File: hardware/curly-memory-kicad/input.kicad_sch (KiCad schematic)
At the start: 5 parts

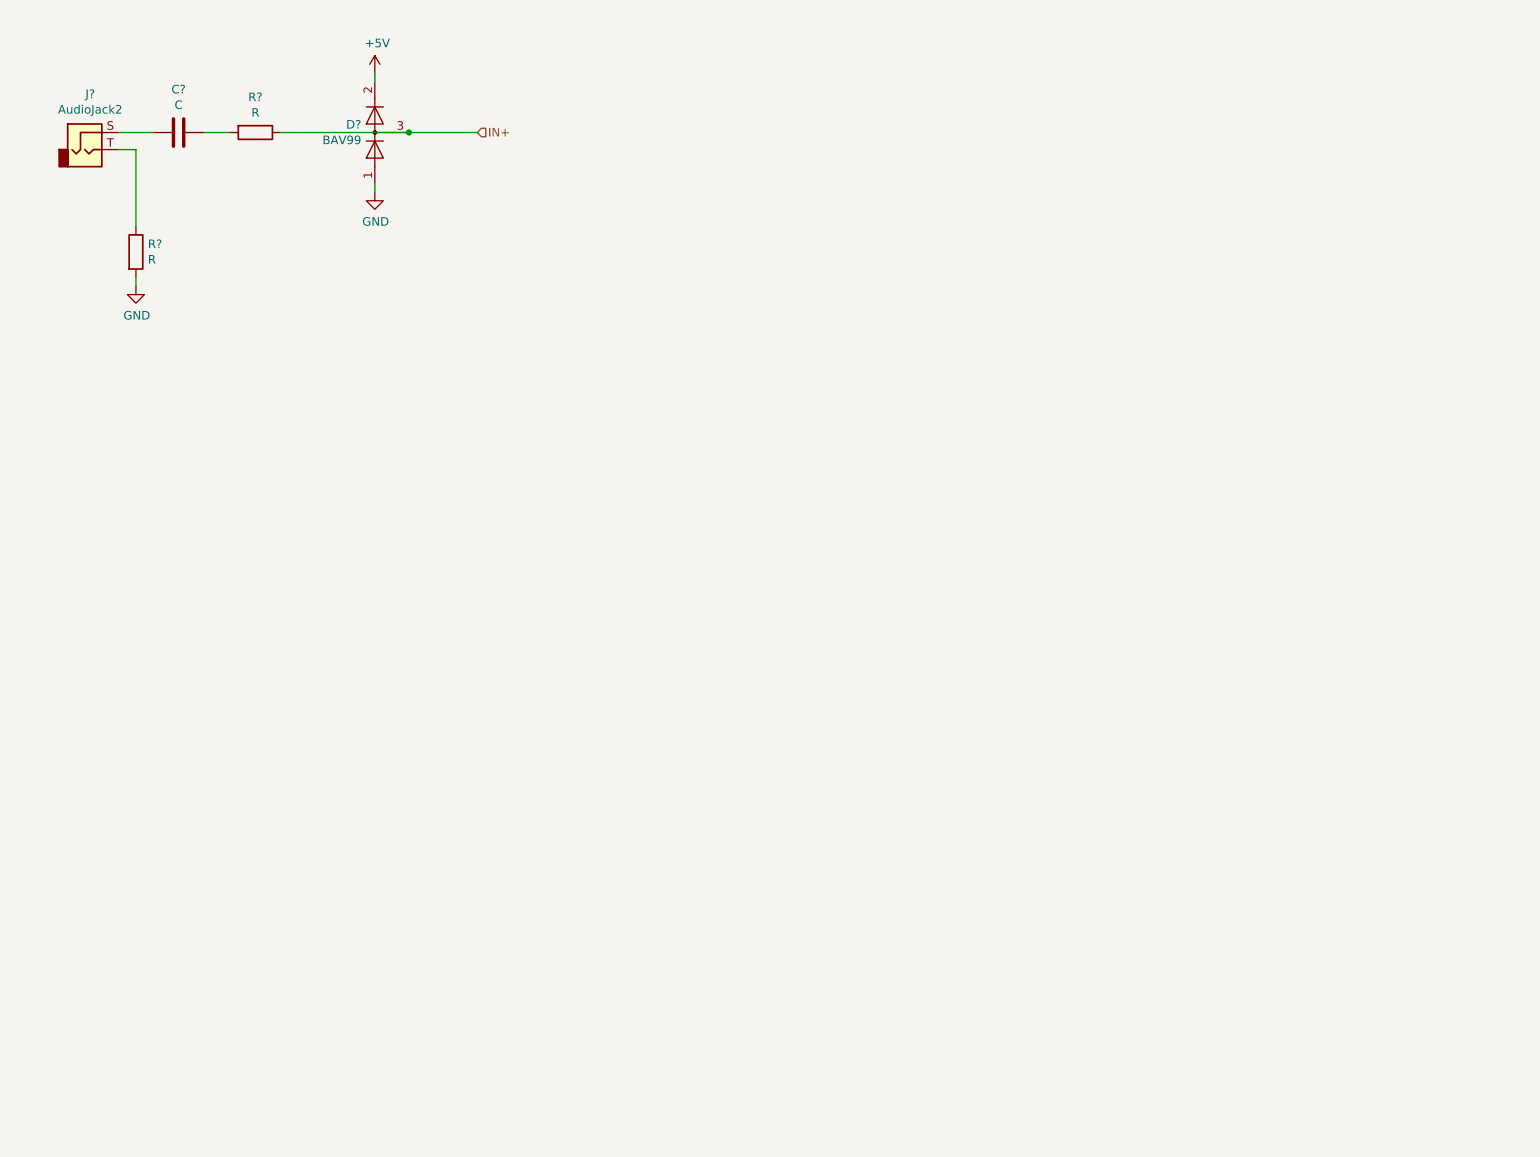
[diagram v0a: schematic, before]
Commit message: output + input op amps added, simuatlion added to sim folder
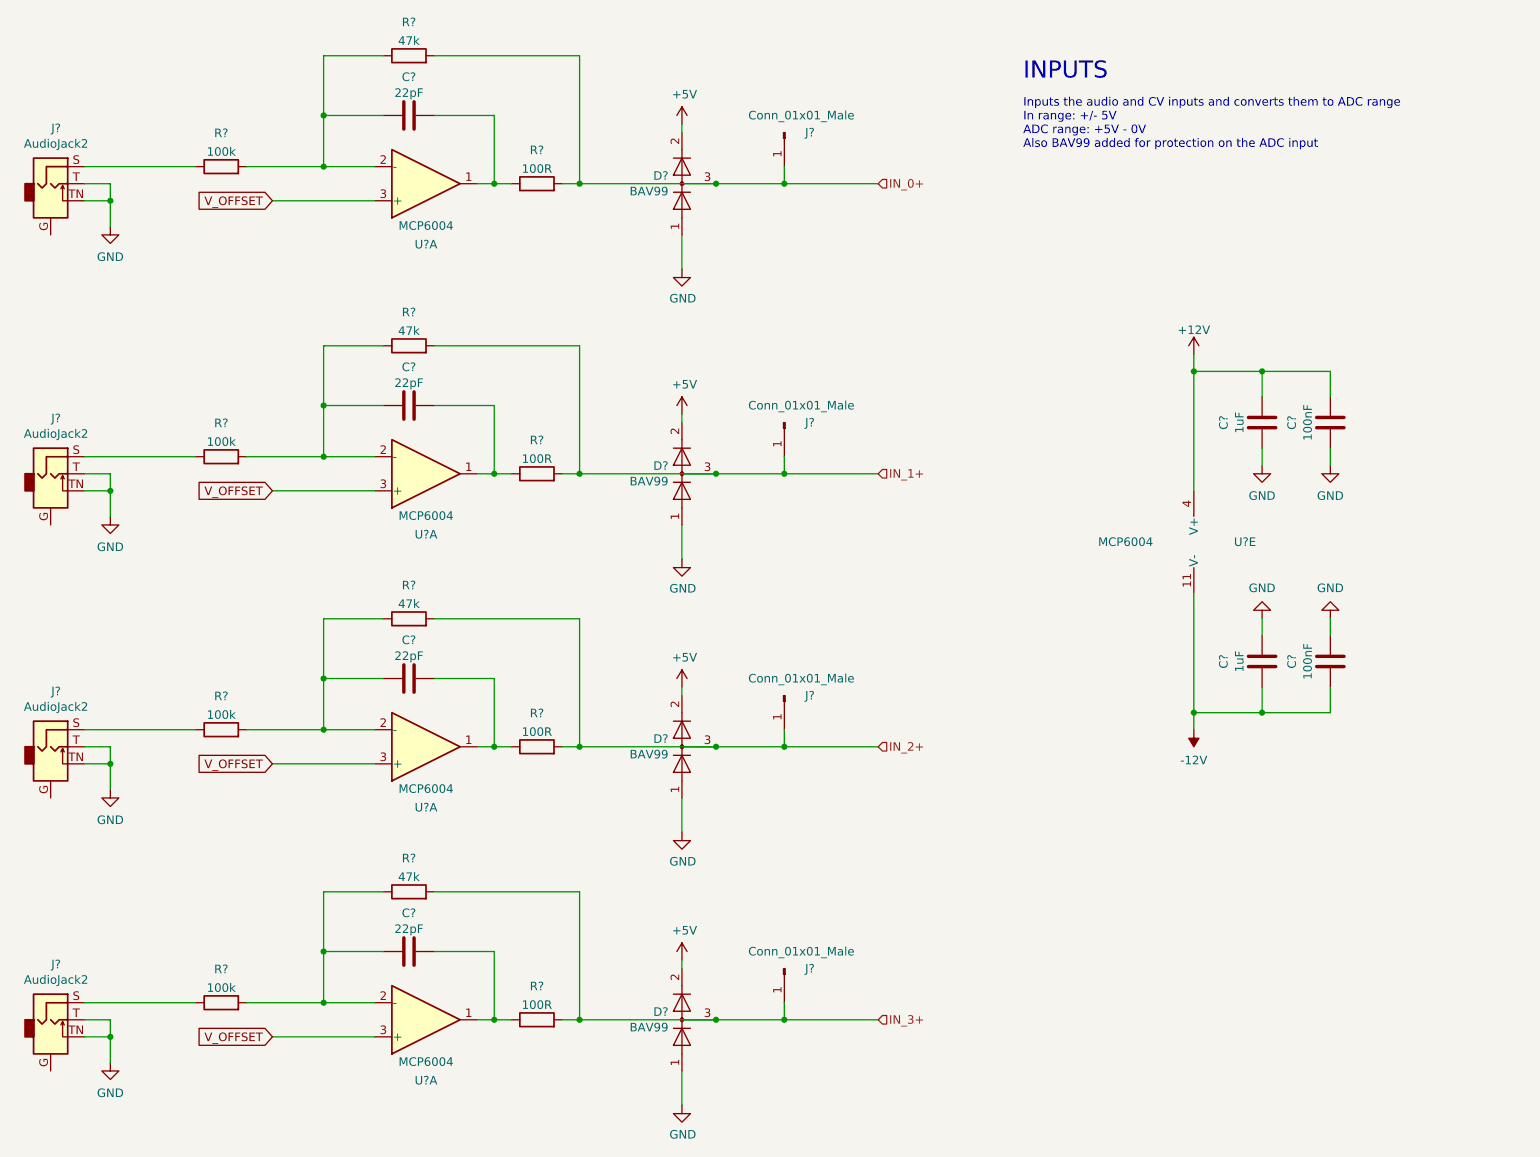
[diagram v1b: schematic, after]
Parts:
- removed C?: C, symbol Device:C
- removed R? (x2): R, symbol Device:R
- added C? (x4): 22pF, symbol Device:C
- added C? (x2): 100nF, symbol Device:C
- added C? (x2): 1uF, symbol Device:C
- added D? (x3): BAV99, Package_TO_SOT_SMD:SOT-23, symbol Diode:BAV99
- added J? (x3): AudioJack2, symbol Connector:AudioJack2_Ground_SwitchT
- added J? (x4): Conn_01x01_Male, Connector_PinSocket_2.54mm:PinSocket_1x01_P2.54mm_Vertical, symbol Connector:Conn_01x01_Male
- added R? (x4): 47k, Resistor_THT:R_Axial_DIN0309_L9.0mm_D3.2mm_P12.70mm_Horizontal, symbol Device:R
- added R? (x4): 100R, Resistor_THT:R_Axial_DIN0309_L9.0mm_D3.2mm_P12.70mm_Horizontal, symbol Device:R
- added R? (x4): 100k, Resistor_THT:R_Axial_DIN0309_L9.0mm_D3.2mm_P12.70mm_Horizontal, symbol Device:R
- added U? (x5): MCP6004, symbol Amplifier_Operational:MCP6004
- J?: symbol Connector:AudioJack2 -> Connector:AudioJack2_Ground_SwitchT
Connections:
- net +5V: now also D?.2 (A), D?.2 (A), D?.2 (A)
- net GND: now also J?.T, J?.TN, C?.2, C?.2, C?.2, C?.2, D?.1 (K), D?.1 (K), D?.1 (K), J?.T, J?.T, J?.T, J?.TN, J?.TN, J?.TN
- net at J?.S: now also R?.1
- net IN+ renamed IN_0+
- net IN_0+: now also J?.1 (Pin_1), R?.2, R?.2
- new net: J?.S, R?.1 (x3)
- new net: C?.2, R?.1, R?.2, U?.2 (-) (x4)
- new net: C?.1, R?.1, U?.1 (x4)
- new net +12V: C?.1, C?.1, U?.4 (V+)
- new net -12V: C?.1, C?.1, U?.11 (V-)
- new net IN_1+: D?.3 (K), J?.1 (Pin_1), R?.2, R?.2
- new net IN_2+: D?.3 (K), J?.1 (Pin_1), R?.2, R?.2
- new net IN_3+: D?.3 (K), J?.1 (Pin_1), R?.2, R?.2
- new net V_OFFSET: U?.3 (+), U?.3 (+), U?.3 (+), U?.3 (+)
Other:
- note added: "INPUTS"
- note added: "Inputs the audio and CV inputs and converts them to ADC range In range: +/- 5V ADC range: +5V - 0V Also BAV99 added for protection on the ADC input"
- moved on the sheet: D?

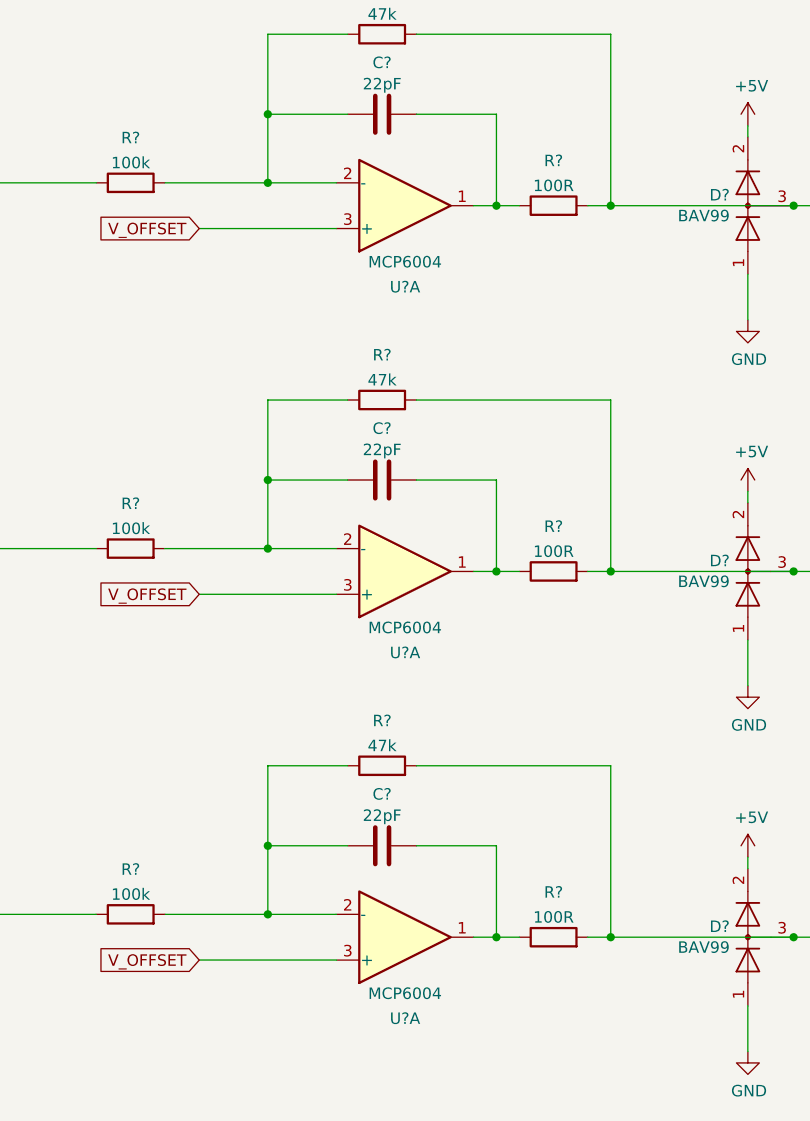
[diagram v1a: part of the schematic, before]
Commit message: schematic updated with component fields on more components
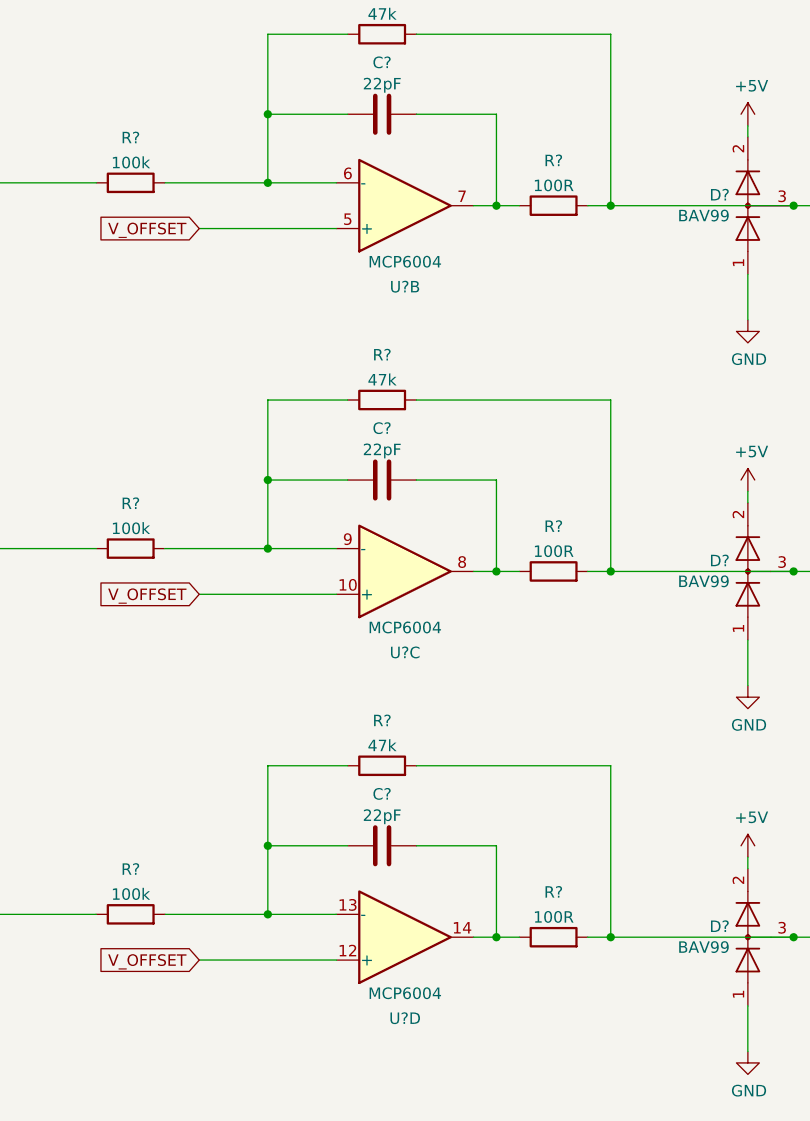
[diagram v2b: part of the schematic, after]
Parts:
- C? (x8): footprint (none) -> Capacitor_SMD:C_0805_2012Metric_Pad1.18x1.45mm_HandSolder
- J? (x4): footprint (none) -> AudioJacks:Jack_3.5mm_QingPu_WQP-PJ398SM_Vertical
- R? (x12): footprint Resistor_THT:R_Axial_DIN0309_L9.0mm_D3.2mm_P12.70mm_Horizontal -> Resistor_SMD:R_0805_2012Metric_Pad1.20x1.40mm_HandSolder
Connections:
- net V_OFFSET: now also U?.10 (+), U?.12 (+), U?.5 (+); no longer U?.3 (+), U?.3 (+), U?.3 (+)
- net at C?.2, R?.1, R?.2: now also U?.9 (-); no longer U?.2 (-)
- net at C?.2, R?.1, R?.2: now also U?.13 (-); no longer U?.2 (-)
- net at C?.1, R?.1: now also U?.14; no longer U?.1
- net at C?.2, R?.1, R?.2: now also U?.6 (-); no longer U?.2 (-)
- net at C?.1, R?.1: now also U?.7; no longer U?.1
- net at C?.1, R?.1: now also U?.8; no longer U?.1

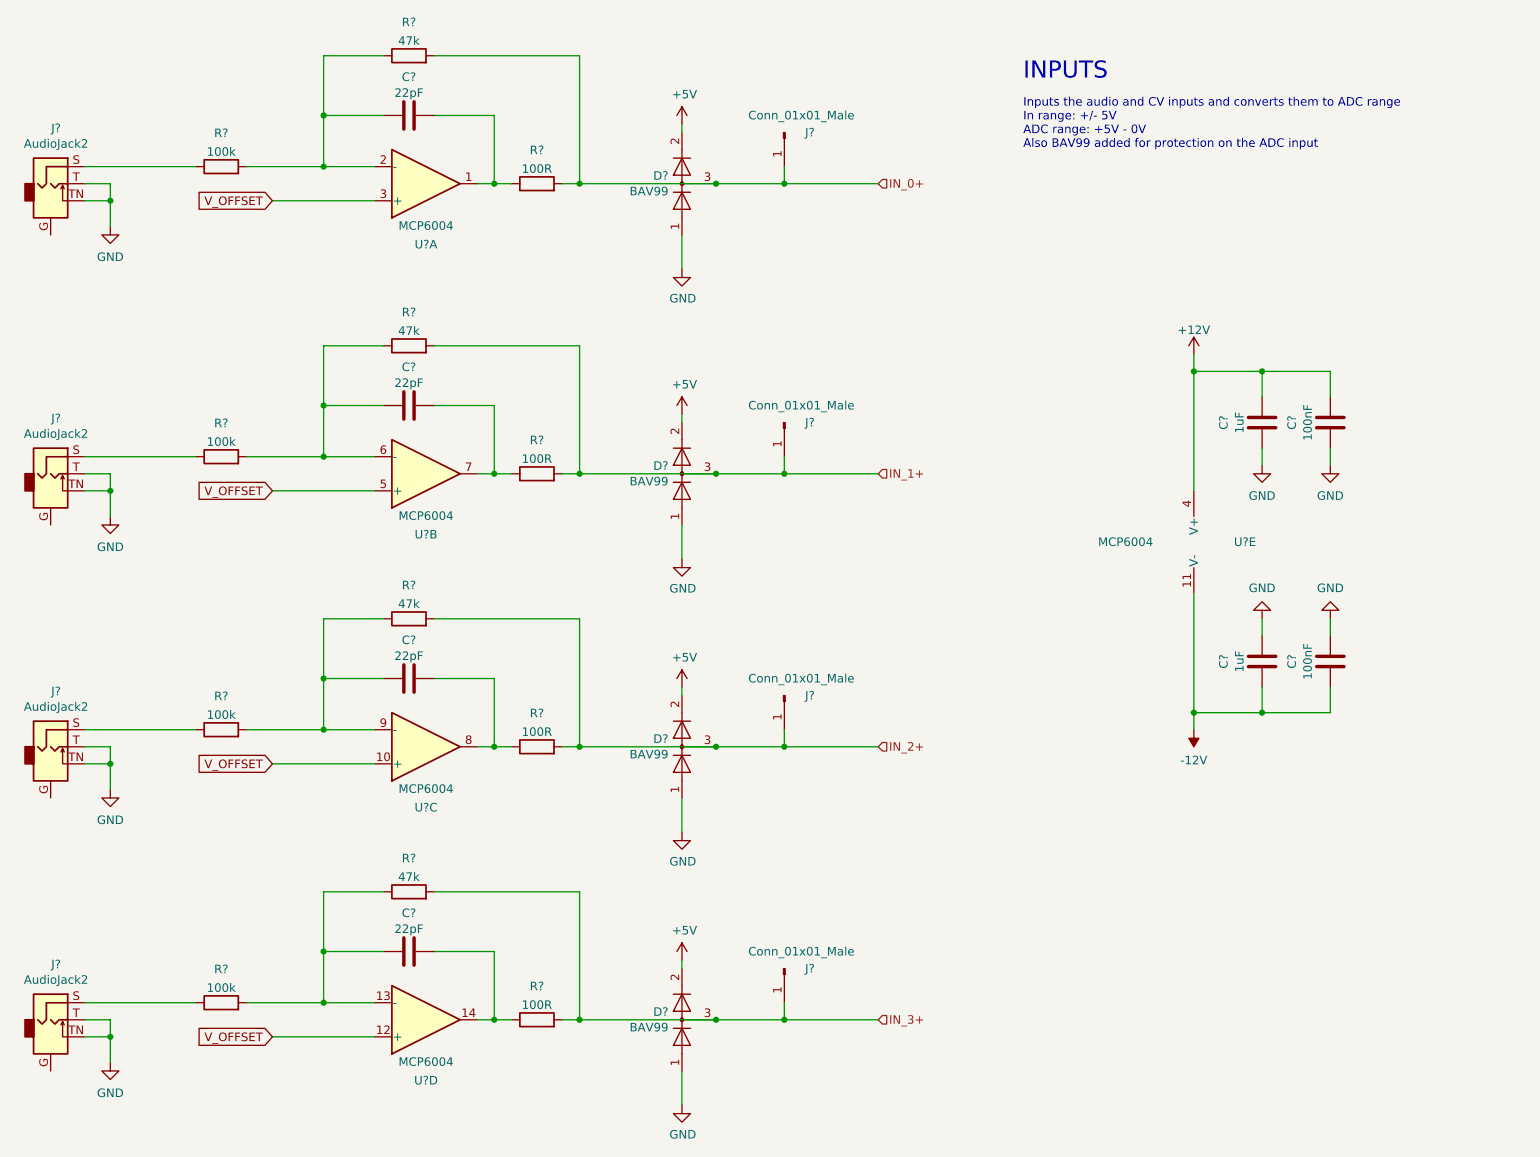
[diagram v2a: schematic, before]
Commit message: all components have part numbers
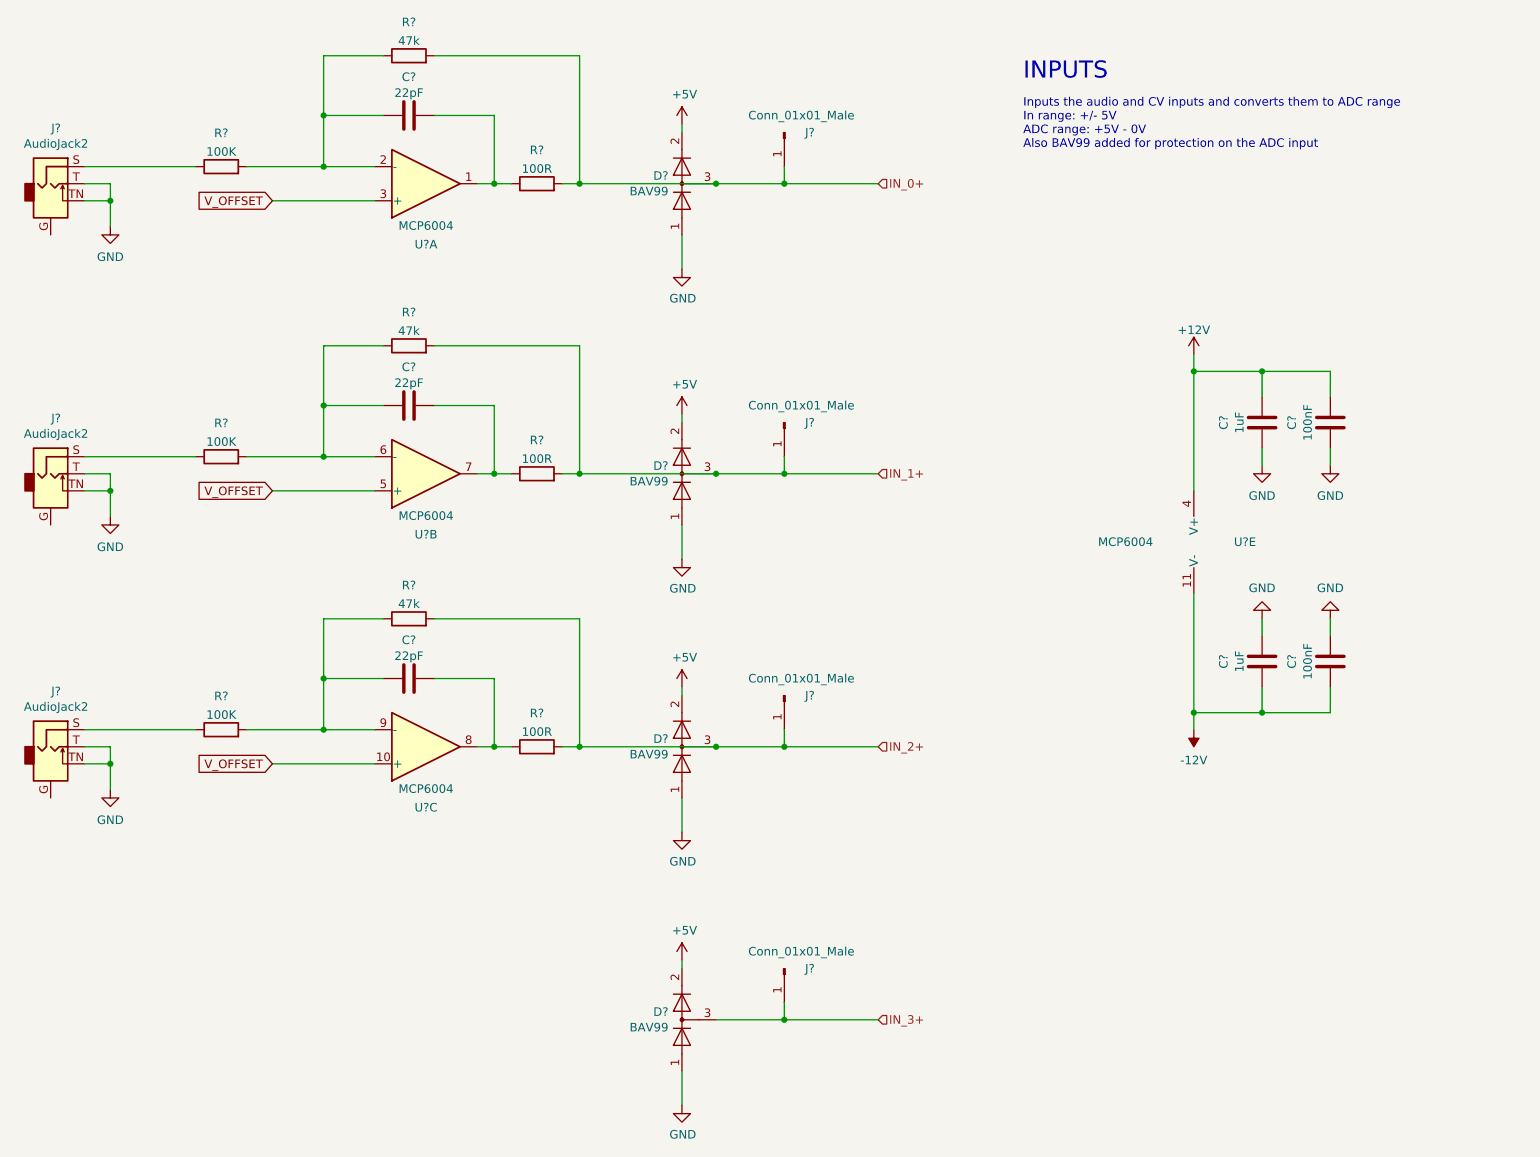
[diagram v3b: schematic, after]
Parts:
- removed C?: 22pF, Capacitor_SMD:C_0805_2012Metric_Pad1.18x1.45mm_HandSolder, symbol Device:C
- removed J?: AudioJack2, AudioJacks:Jack_3.5mm_QingPu_WQP-PJ398SM_Vertical, symbol Connector:AudioJack2_Ground_SwitchT
- removed R?: 47k, Resistor_SMD:R_0805_2012Metric_Pad1.20x1.40mm_HandSolder, symbol Device:R
- removed R?: 100R, Resistor_SMD:R_0805_2012Metric_Pad1.20x1.40mm_HandSolder, symbol Device:R
- removed R?: 100k, Resistor_SMD:R_0805_2012Metric_Pad1.20x1.40mm_HandSolder, symbol Device:R
- removed U?: MCP6004, symbol Amplifier_Operational:MCP6004
- R? (x3): value 100k -> 100K
- U? (x4): footprint (none) -> Package_SO:SOIC-14_3.9x8.7mm_P1.27mm
